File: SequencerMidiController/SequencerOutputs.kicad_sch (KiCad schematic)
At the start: 31 parts, among them J4 Conn_02x10_Odd_Even, U34 ADG2188

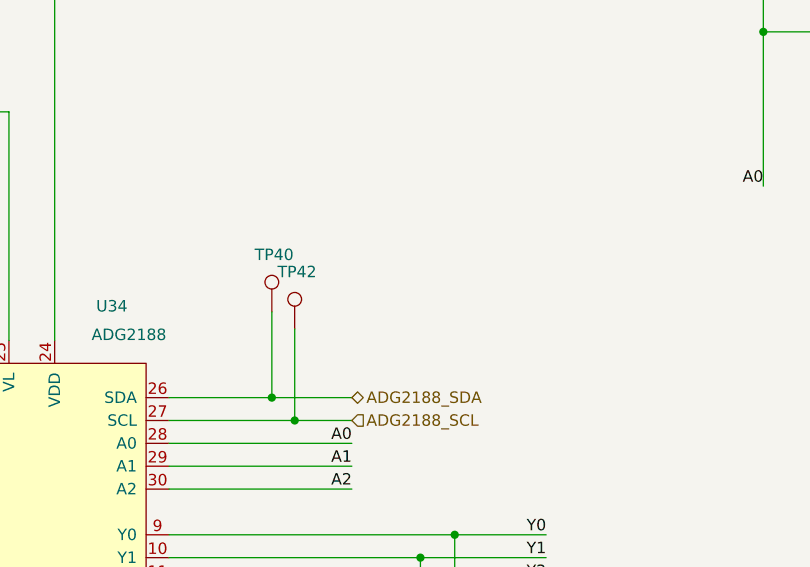
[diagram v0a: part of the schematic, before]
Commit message: Add ground points
https://github.com/cracked-machine/BassStationSequencerMidiController/issues/9

Also, made space on layout for uSDCard IDC connector and DAC analog output section
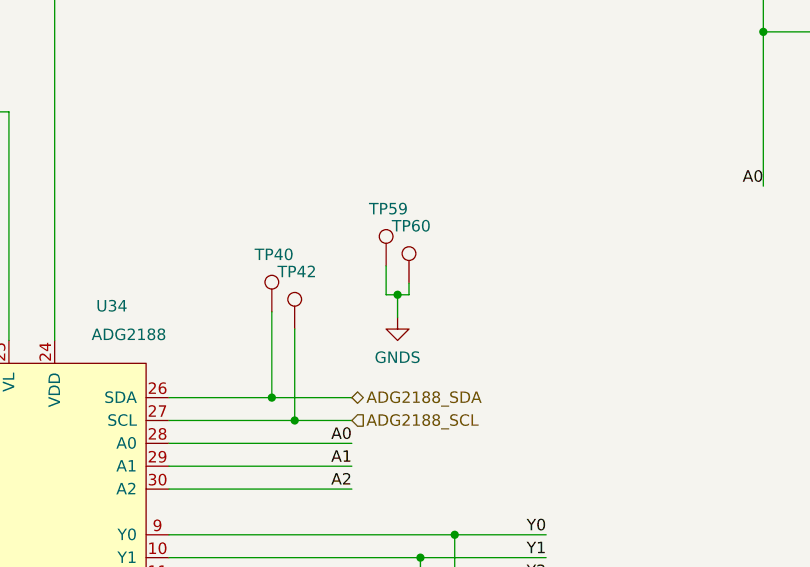
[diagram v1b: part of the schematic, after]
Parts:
- added TP59, TP60: TestPoint, TestPoint:TestPoint_Pad_D1.0mm, symbol Connector:TestPoint
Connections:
- net GNDS: now also TP59.1, TP60.1
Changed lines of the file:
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@@
   (junction (at 134.62 92.075) (diameter 0) (color 0 0 0 0)
+  )
+  (junction (at 146.05 78.105) (diameter 0) (color 0 0 0 0)
   )
   (junction (at 219.075 54.61) (diameter 0) (color 0 0 0 0)
@@
     (stroke (width 0) (type default) (color 0 0 0 0))
   )
+  (wire (pts (xy 144.78 74.93) (xy 144.78 78.105))
+    (stroke (width 0) (type default) (color 0 0 0 0))
+  )
   (wire (pts (xy 132.08 89.535) (xy 132.08 80.01))
     (stroke (width 0) (type default) (color 0 0 0 0))
@@
     (stroke (width 0) (type default) (color 0 0 0 0))
   )
+  (wire (pts (xy 147.32 78.105) (xy 147.32 76.835))
+    (stroke (width 0) (type default) (color 0 0 0 0))
+  )
   (wire (pts (xy 148.59 107.315) (xy 162.56 107.315))
     (stroke (width 0) (type default) (color 0 0 0 0))
@@
     (stroke (width 0) (type default) (color 0 0 0 0))
   )
+  (wire (pts (xy 144.78 78.105) (xy 146.05 78.105))
+    (stroke (width 0) (type default) (color 0 0 0 0))
+  )
   (wire (pts (xy 144.78 109.855) (xy 162.56 109.855))
     (stroke (width 0) (type default) (color 0 0 0 0))
@@
     (stroke (width 0) (type default) (color 0 0 0 0))
   )
+  (wire (pts (xy 146.05 78.105) (xy 147.32 78.105))
+    (stroke (width 0) (type default) (color 0 0 0 0))
+  )
   (wire (pts (xy 129.54 120.015) (xy 129.54 140.335))
     (stroke (width 0) (type default) (color 0 0 0 0))
@@
   )
   (wire (pts (xy 76.2 109.855) (xy 90.17 109.855))
+    (stroke (width 0) (type default) (color 0 0 0 0))
+  )
+  (wire (pts (xy 146.05 78.105) (xy 146.05 80.645))
     (stroke (width 0) (type default) (color 0 0 0 0))
   )
@@
       (effects (font (size 1.27 1.27)) hide)
     )
+    (pin "1")
+  )
+  (symbol (lib_id "Connector:TestPoint") (at 147.32 76.835 0) (unit 1)
+    (in_bom yes) (on_board yes)
+    (property "Reference" "TP60" (id 0) (at 145.415 70.485 0)
+      (effects (font (size 1.27 1.27)) (justify left))
+    )
+    (property "Value" "TestPoint" (id 1) (at 148.7932 76.1492 0)
+      (effects (font (size 1.27 1.27)) (justify left) hide)
+    )
+    (property "Footprint" "TestPoint:TestPoint_Pad_D1.0mm" (id 2) (at 152.4 76.835 0)
+      (effects (font (size 1.27 1.27)) hide)
+    )
+    (property "Datasheet" "~" (id 3) (at 152.4 76.835 0)
+      (effects (font (size 1.27 1.27)) hide)
+    )
+    (property "LcscNo" "~" (id 4) (at 147.32 76.835 0)
+      (effects (font (size 1.27 1.27)) hide)
+    )
+    (property "Type" "~" (id 5) (at 147.32 76.835 0)
+      (effects (font (size 1.27 1.27)) hide)
+    )
+    (pin "1")
+  )
+  (symbol (lib_id "Connector:TestPoint") (at 144.78 74.93 0) (unit 1)
+    (in_bom yes) (on_board yes)
+    (property "Reference" "TP59" (id 0) (at 142.875 68.58 0)
+      (effects (font (size 1.27 1.27)) (justify left))
+    )
+    (property "Value" "TestPoint" (id 1) (at 146.2532 74.2442 0)
+      (effects (font (size 1.27 1.27)) (justify left) hide)
+    )
+    (property "Footprint" "TestPoint:TestPoint_Pad_D1.0mm" (id 2) (at 149.86 74.93 0)
+      (effects (font (size 1.27 1.27)) hide)
+    )
+    (property "Datasheet" "~" (id 3) (at 149.86 74.93 0)
+      (effects (font (size 1.27 1.27)) hide)
+    )
+    (property "LcscNo" "~" (id 4) (at 144.78 74.93 0)
+      (effects (font (size 1.27 1.27)) hide)
+    )
+    (property "Type" "~" (id 5) (at 144.78 74.93 0)
+      (effects (font (size 1.27 1.27)) hide)
+    )
+    (pin "1")
+  )
+  (symbol (lib_id "power:GNDS") (at 146.05 80.645 0) (unit 1)
+    (in_bom yes) (on_board yes) (fields_autoplaced)
+    (property "Reference" "#PWR038" (id 0) (at 146.05 86.995 0)
+      (effects (font (size 1.27 1.27)) hide)
+    )
+    (property "Value" "GNDS" (id 1) (at 146.05 85.09 0))
+    (property "Footprint" "" (id 2) (at 146.05 80.645 0)
+      (effects (font (size 1.27 1.27)) hide)
+    )
+    (property "Datasheet" "" (id 3) (at 146.05 80.645 0)
+      (effects (font (size 1.27 1.27)) hide)
+    )
